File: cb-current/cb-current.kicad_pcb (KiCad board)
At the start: 4 copper layers, 55 x 40 mm, 35 parts, among them P1 CONN_3, P2 CONN_3, P3 CONN_3, P4 CONN_01X09, P5 CONN_01X02, P6 CONN_01X01, P7 CONN_01X01, P8 CONN_01X01, SW1 SW_PUSH_SMALL, U1 MCP1700-3.0

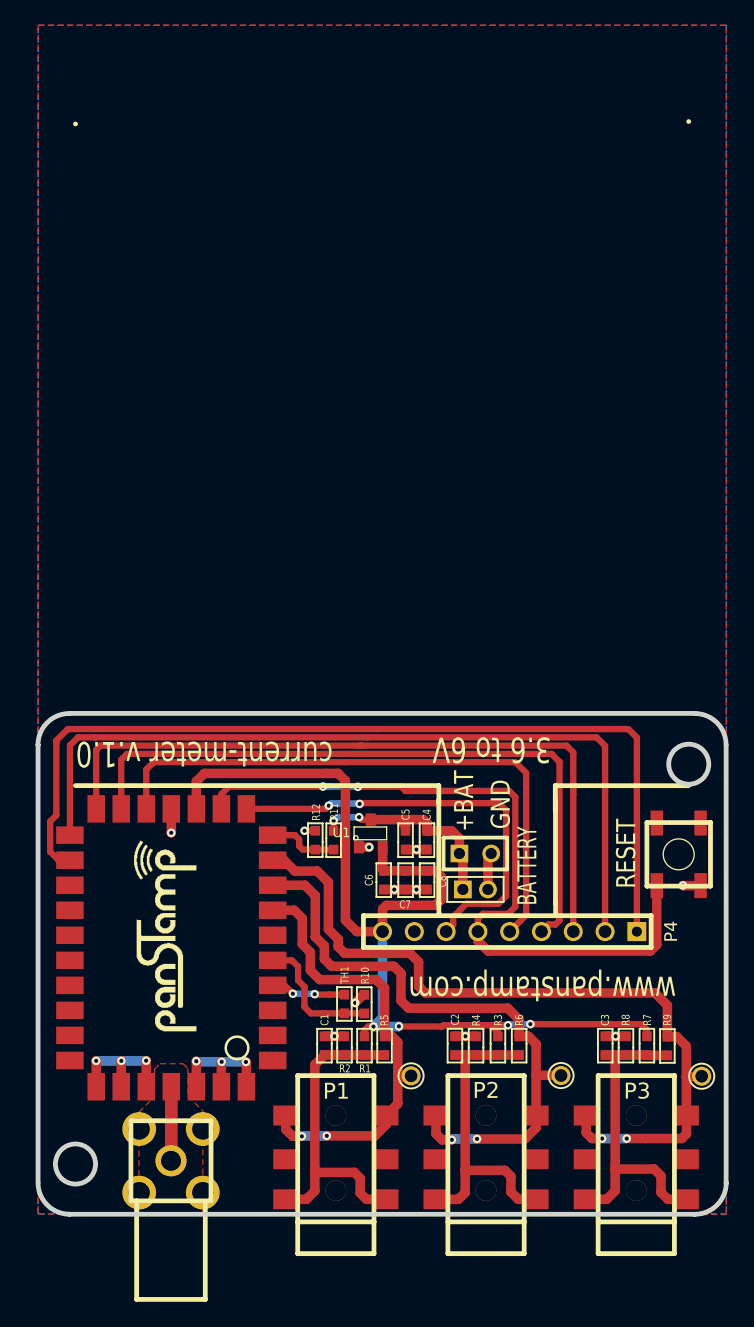
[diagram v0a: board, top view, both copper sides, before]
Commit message: Drive current circuits from MCU pins
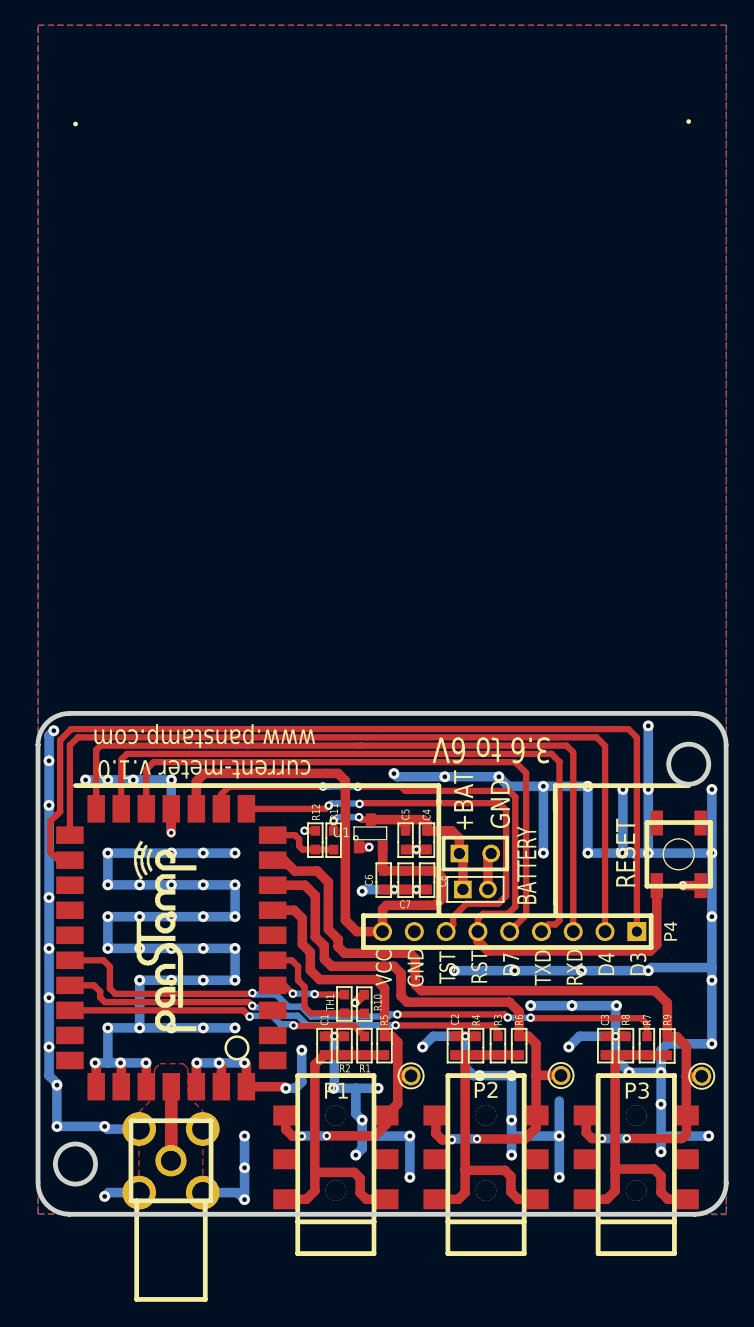
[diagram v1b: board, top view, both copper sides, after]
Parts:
- R11, R12: value 470k -> 1M
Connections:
- R1 pad 2: VCC -> /D20
- R3 pad 2: VCC -> /D21
- R7 pad 2: VCC -> /D22
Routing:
- net GND: track 39.5 -> 360.5 mm, vias 17 -> 110
- net /D22: track 0.00 -> 50.4 mm, vias 0 -> 4
- net VCC: track 87.2 -> 44.4 mm, vias 4 -> 0
- net /D21: track 0.00 -> 36.4 mm, vias 0 -> 2
- net /D20: track 0.00 -> 24.4 mm, vias 0 -> 2
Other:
- board text added: "D3"
- board text added: "D4"
- board text added: "D7"
- board text added: "RST"
- board text added: "RXD"
- board text added: "TST"
- board text added: "TXD"
- board text added: "VCC"
- board text added: "current-meter v.1.0 www.panstamp.com"
- board text removed: "current-meter v.1.0"
- board text removed: "www.panstamp.com"

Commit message: voltage divider resistors changed to 10K for current channels
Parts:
- R1, R2, R3, R4, R7, R8: value 470k -> 10k
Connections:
- P1 pad 2: (no net) -> Net-(P1-Pad2)
- P2 pad 2: (no net) -> Net-(P2-Pad2)
- P3 pad 2: (no net) -> Net-(P3-Pad2)
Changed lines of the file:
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@@
-(kicad_pcb (version 4) (host pcbnew 0.201512201246+6385~39~ubuntu14.04.1-stable)
+(kicad_pcb (version 4) (host pcbnew 4.0.2+dfsg1-stable)
   (general
-    (links 82)
-    (no_connects 0)
+    (links 85)
+    (no_connects 3)
     (area 94.302579 124.795279 149.674581 165.196521)
     (thickness 1.6002)
@@
     (zones 0)
     (modules 35)
-    (nets 33)
+    (nets 36)
   )
   (page A4)
   (title_block
     (title "Current meter board for panStamp 2")
-    (date "15 Apr 2015")
-    (rev 1.0)
+    (date 2017-03-14)
+    (rev 1.1)
     (company panStamp)
   )
@@
   )
   (setup
-    (last_trace_width 0.762)
+    (last_trace_width 0.1524)
     (user_trace_width 0.2032)
     (user_trace_width 0.254)
@@
   (net 31 /A4)
   (net 32 /A0)
+  (net 33 "Net-(P1-Pad2)")
+  (net 34 "Net-(P2-Pad2)")
+  (net 35 "Net-(P3-Pad2)")
   (net_class Default "This is the default net class."
     (clearance 0.1524)
@@
     (add_net "Net-(C2-Pad1)")
     (add_net "Net-(C3-Pad1)")
+    (add_net "Net-(P1-Pad2)")
+    (add_net "Net-(P2-Pad2)")
+    (add_net "Net-(P3-Pad2)")
     (add_net VCC)
   )
@@
     (pad 1 smd rect (at -4.0005 3.27914) (size 1.99898 1.6002) (layers Front F.Paste F.Mask)
       (net 25 "Net-(C2-Pad1)"))
-    (pad 2 smd rect (at -4.0005 0.07874) (size 1.99898 1.6002) (layers Front F.Paste F.Mask))
+    (pad 2 smd rect (at -4.0005 0.07874) (size 1.99898 1.6002) (layers Front F.Paste F.Mask)
+      (net 34 "Net-(P2-Pad2)"))
     (pad 3 smd rect (at -4.0005 -3.41884) (size 1.99898 1.6002) (layers Front F.Paste F.Mask)
       (net 29 /A2))
     (pad 1 smd rect (at 4.0005 3.27914) (size 1.99898 1.6002) (layers Front F.Paste F.Mask)
       (net 25 "Net-(C2-Pad1)"))
-    (pad 2 smd rect (at 4.0005 0.07874) (size 1.99898 1.6002) (layers Front F.Paste F.Mask))
+    (pad 2 smd rect (at 4.0005 0.07874) (size 1.99898 1.6002) (layers Front F.Paste F.Mask)
+      (net 34 "Net-(P2-Pad2)"))
     (pad 3 smd rect (at 4.0005 -3.41884) (size 1.99898 1.6002) (layers Front F.Paste F.Mask)
       (net 29 /A2))
@@
     (pad 1 smd rect (at -4.0005 3.27914) (size 1.99898 1.6002) (layers Front F.Paste F.Mask)
       (net 26 "Net-(C3-Pad1)"))
-    (pad 2 smd rect (at -4.0005 0.07874) (size 1.99898 1.6002) (layers Front F.Paste F.Mask))
+    (pad 2 smd rect (at -4.0005 0.07874) (size 1.99898 1.6002) (layers Front F.Paste F.Mask)
+      (net 35 "Net-(P3-Pad2)"))
     (pad 3 smd rect (at -4.0005 -3.41884) (size 1.99898 1.6002) (layers Front F.Paste F.Mask)
       (net 30 /A1))
     (pad 1 smd rect (at 4.0005 3.27914) (size 1.99898 1.6002) (layers Front F.Paste F.Mask)
       (net 26 "Net-(C3-Pad1)"))
-    (pad 2 smd rect (at 4.0005 0.07874) (size 1.99898 1.6002) (layers Front F.Paste F.Mask))
+    (pad 2 smd rect (at 4.0005 0.07874) (size 1.99898 1.6002) (layers Front F.Paste F.Mask)
+      (net 35 "Net-(P3-Pad2)"))
     (pad 3 smd rect (at 4.0005 -3.41884) (size 1.99898 1.6002) (layers Front F.Paste F.Mask)
       (net 30 /A1))
@@
     (pad 1 smd rect (at -4.0005 3.27914) (size 1.99898 1.6002) (layers Front F.Paste F.Mask)
       (net 1 "Net-(C1-Pad1)"))
-    (pad 2 smd rect (at -4.0005 0.07874) (size 1.99898 1.6002) (layers Front F.Paste F.Mask))
+    (pad 2 smd rect (at -4.0005 0.07874) (size 1.99898 1.6002) (layers Front F.Paste F.Mask)
+      (net 33 "Net-(P1-Pad2)"))
     (pad 3 smd rect (at -4.0005 -3.41884) (size 1.99898 1.6002) (layers Front F.Paste F.Mask)
       (net 28 /A3))
     (pad 1 smd rect (at 4.0005 3.27914) (size 1.99898 1.6002) (layers Front F.Paste F.Mask)
       (net 1 "Net-(C1-Pad1)"))
-    (pad 2 smd rect (at 4.0005 0.07874) (size 1.99898 1.6002) (layers Front F.Paste F.Mask))
+    (pad 2 smd rect (at 4.0005 0.07874) (size 1.99898 1.6002) (layers Front F.Paste F.Mask)
+      (net 33 "Net-(P1-Pad2)"))
     (pad 3 smd rect (at 4.0005 -3.41884) (size 1.99898 1.6002) (layers Front F.Paste F.Mask)
       (net 28 /A3))
@@
       (effects (font (size 0.635 0.508) (thickness 0.127)))
     )
-    (fp_text value 470k (at 0.0762 -0.0254 90) (layer F.SilkS) hide
+    (fp_text value 10k (at 0.0762 -0.0254 90) (layer F.SilkS) hide
       (effects (font (size 0.635 0.508) (thickness 0.127)))
     )
@@
       (effects (font (size 0.635 0.508) (thickness 0.127)))
     )
-    (fp_text value 470k (at 0.0762 -0.0254 270) (layer F.SilkS) hide
+    (fp_text value 10k (at 0.0762 -0.0254 270) (layer F.SilkS) hide
       (effects (font (size 0.635 0.508) (thickness 0.127)))
     )
@@
       (effects (font (size 0.635 0.508) (thickness 0.127)))
     )
-    (fp_text value 470k (at 0.0762 -0.0254 90) (layer F.SilkS) hide
+    (fp_text value 10k (at 0.0762 -0.0254 90) (layer F.SilkS) hide
       (effects (font (size 0.635 0.508) (thickness 0.127)))
     )
@@
       (effects (font (size 0.635 0.508) (thickness 0.127)))
     )
-    (fp_text value 470k (at 0.0762 -0.0254 270) (layer F.SilkS) hide
+    (fp_text value 10k (at 0.0762 -0.0254 270) (layer F.SilkS) hide
       (effects (font (size 0.635 0.508) (thickness 0.127)))
     )
@@
       (effects (font (size 0.635 0.508) (thickness 0.127)))
     )
-    (fp_text value 470k (at 0.0762 -0.0254 90) (layer F.SilkS) hide
+    (fp_text value 10k (at 0.0762 -0.0254 90) (layer F.SilkS) hide
       (effects (font (size 0.635 0.508) (thickness 0.127)))
     )
@@
       (effects (font (size 0.635 0.508) (thickness 0.127)))
     )
-    (fp_text value 470k (at 0.0762 -0.0254 270) (layer F.SilkS) hide
-      (effects (font (size 0.635 0.508) (thickness 0.127)))
-    )
+    (fp_text value 10k (at 0.0762 -0.0254 270) (layer F.SilkS) hide
+      (effects (font (size 0.635 0.508) (thickness 0.127)))
+    )
